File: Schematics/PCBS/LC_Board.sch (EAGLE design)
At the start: 7 parts, among them IC1 STP16C596M

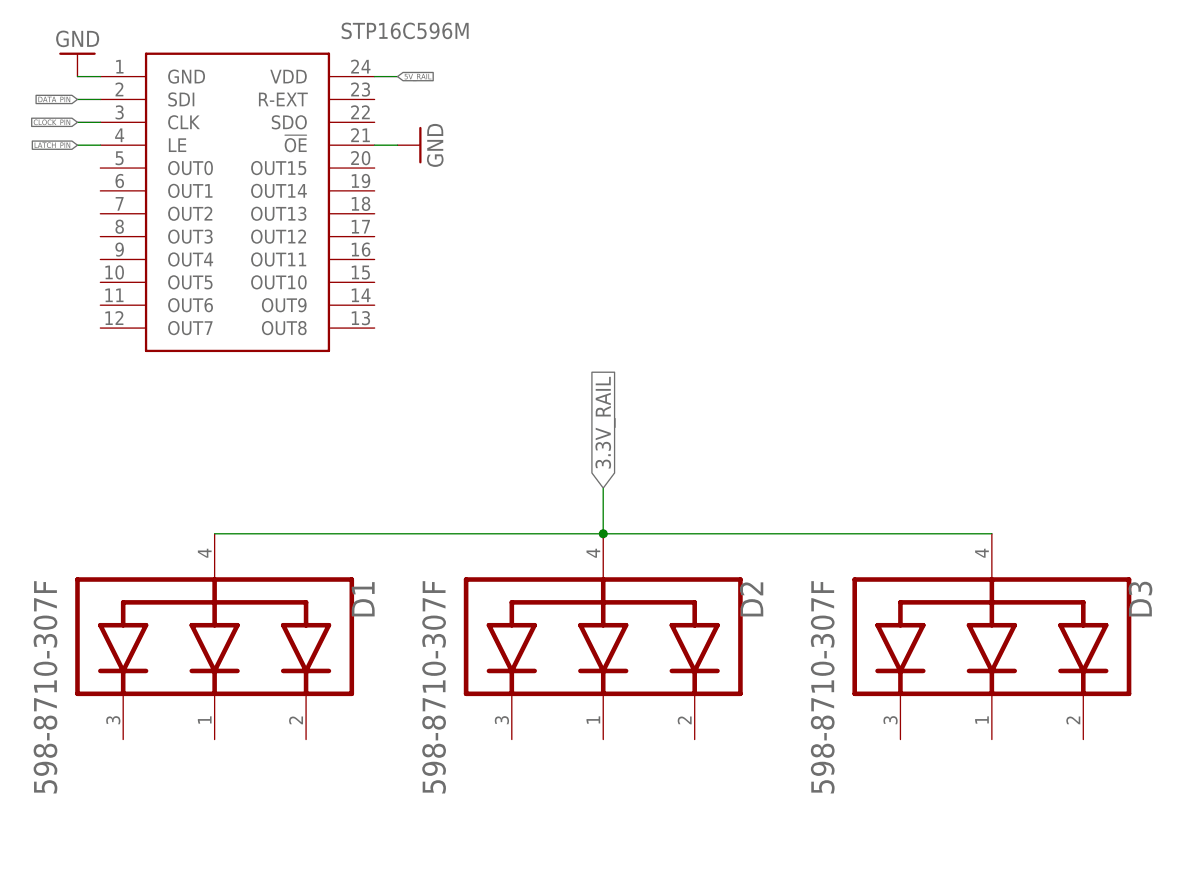
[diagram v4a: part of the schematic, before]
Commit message: connected LED & IO to Shift register
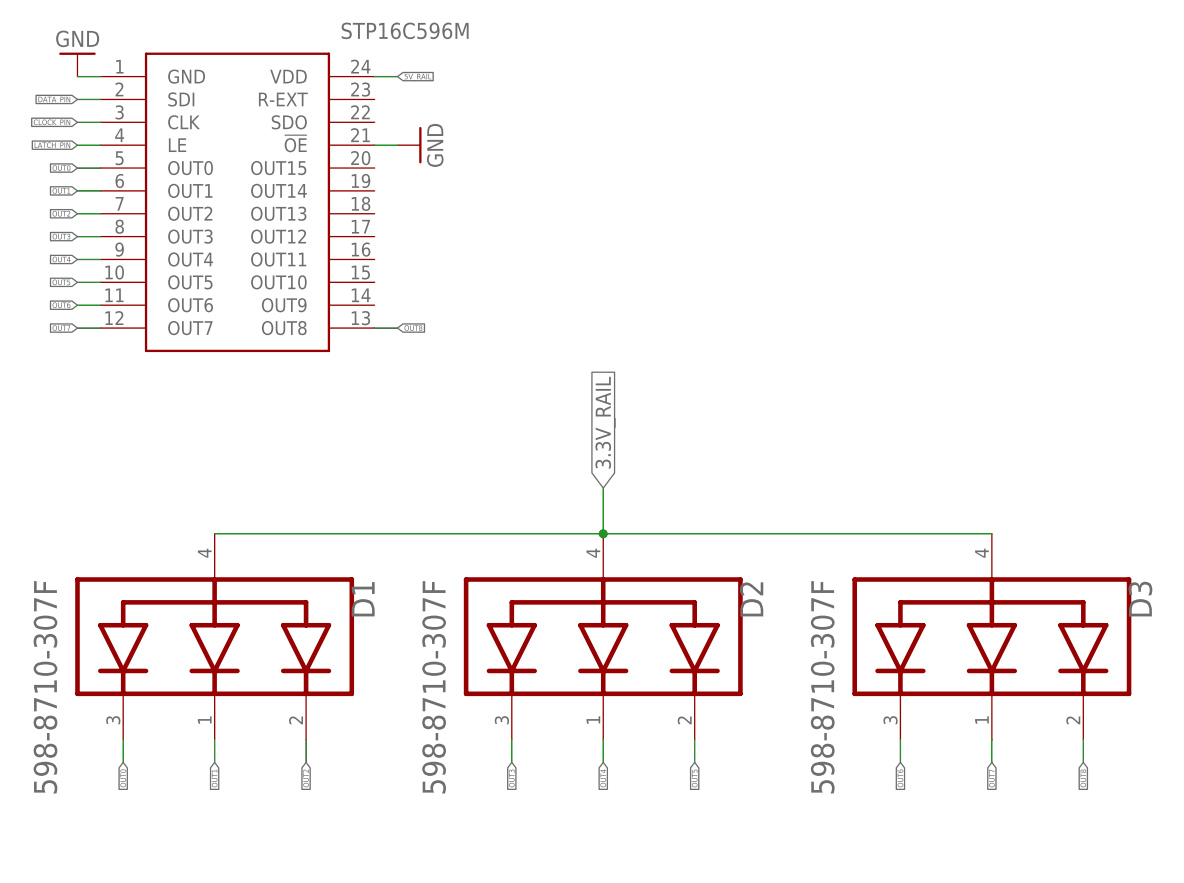
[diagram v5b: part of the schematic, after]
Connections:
- new net OUT0: D1.BLUE_CATHODE, IC1.OUT0
- new net OUT1: D1.GREEN_CATHODE, IC1.OUT1
- new net OUT2: D1.RED_CATHODE, IC1.OUT2
- new net OUT3: D2.BLUE_CATHODE, IC1.OUT3
- new net OUT4: D2.GREEN_CATHODE, IC1.OUT4
- new net OUT5: D2.RED_CATHODE, IC1.OUT5
- new net OUT6: D3.BLUE_CATHODE, IC1.OUT6
- new net OUT7: D3.GREEN_CATHODE, IC1.OUT7
- new net OUT8: D3.RED_CATHODE, IC1.OUT8
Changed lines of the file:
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@@
+</segment>
+</net>
+<net name="OUT0" class="0">
+<segment>
+<pinref part="IC1" gate="G$1" pin="OUT0"/>
+<wire x1="510.54" y1="0" x2="508" y2="0" width="0.1524" layer="91"/>
+<label x="508" y="0" size="0.6096" layer="95" rot="R180" xref="yes"/>
+</segment>
+<segment>
+<pinref part="D1" gate="G$0" pin="BLUE_CATHODE"/>
+<wire x1="513.08" y1="-63.5" x2="513.08" y2="-66.04" width="0.1524" layer="91"/>
+<label x="513.08" y="-66.04" size="0.6096" layer="95" rot="R270" xref="yes"/>
+</segment>
+</net>
+<net name="OUT1" class="0">
+<segment>
+<pinref part="IC1" gate="G$1" pin="OUT1"/>
+<wire x1="510.54" y1="-2.54" x2="508" y2="-2.54" width="0.1524" layer="91"/>
+<label x="508" y="-2.54" size="0.6096" layer="95" rot="R180" xref="yes"/>
+</segment>
+<segment>
+<pinref part="D1" gate="G$0" pin="GREEN_CATHODE"/>
+<wire x1="523.24" y1="-63.5" x2="523.24" y2="-66.04" width="0.1524" layer="91"/>
+<label x="523.24" y="-66.04" size="0.6096" layer="95" rot="R270" xref="yes"/>
+</segment>
+</net>
+<net name="OUT2" class="0">
+<segment>
+<pinref part="IC1" gate="G$1" pin="OUT2"/>
+<wire x1="510.54" y1="-5.08" x2="508" y2="-5.08" width="0.1524" layer="91"/>
+<label x="508" y="-5.08" size="0.6096" layer="95" rot="R180" xref="yes"/>
+</segment>
+<segment>
+<pinref part="D1" gate="G$0" pin="RED_CATHODE"/>
+<wire x1="533.4" y1="-63.5" x2="533.4" y2="-66.04" width="0.1524" layer="91"/>
+<label x="533.4" y="-66.04" size="0.6096" layer="95" rot="R270" xref="yes"/>
+</segment>
+</net>
+<net name="OUT3" class="0">
+<segment>
+<pinref part="IC1" gate="G$1" pin="OUT3"/>
+<wire x1="510.54" y1="-7.62" x2="508" y2="-7.62" width="0.1524" layer="91"/>
+<label x="508" y="-7.62" size="0.6096" layer="95" rot="R180" xref="yes"/>
+</segment>
+<segment>
+<pinref part="D2" gate="G$0" pin="BLUE_CATHODE"/>
+<wire x1="556.26" y1="-63.5" x2="556.26" y2="-66.04" width="0.1524" layer="91"/>
+<label x="556.26" y="-66.04" size="0.6096" layer="95" rot="R270" xref="yes"/>
+</segment>
+</net>
+<net name="OUT4" class="0">
+<segment>
+<pinref part="IC1" gate="G$1" pin="OUT4"/>
+<wire x1="510.54" y1="-10.16" x2="508" y2="-10.16" width="0.1524" layer="91"/>
+<label x="508" y="-10.16" size="0.6096" layer="95" rot="R180" xref="yes"/>
+</segment>
+<segment>
+<pinref part="D2" gate="G$0" pin="GREEN_CATHODE"/>
+<wire x1="566.42" y1="-63.5" x2="566.42" y2="-66.04" width="0.1524" layer="91"/>
+<label x="566.42" y="-66.04" size="0.6096" layer="95" rot="R270" xref="yes"/>
+</segment>
+</net>
+<net name="OUT5" class="0">
+<segment>
+<pinref part="D2" gate="G$0" pin="RED_CATHODE"/>
+<wire x1="576.58" y1="-63.5" x2="576.58" y2="-66.04" width="0.1524" layer="91"/>
+<label x="576.58" y="-66.04" size="0.6096" layer="95" rot="R270" xref="yes"/>
+</segment>
+<segment>
+<pinref part="IC1" gate="G$1" pin="OUT5"/>
+<wire x1="510.54" y1="-12.7" x2="508" y2="-12.7" width="0.1524" layer="91"/>
+<label x="508" y="-12.7" size="0.6096" layer="95" rot="R180" xref="yes"/>
+</segment>
+</net>
+<net name="OUT7" class="0">
+<segment>
+<pinref part="D3" gate="G$0" pin="GREEN_CATHODE"/>
+<wire x1="609.6" y1="-63.5" x2="609.6" y2="-66.04" width="0.1524" layer="91"/>
+<label x="609.6" y="-66.04" size="0.6096" layer="95" rot="R270" xref="yes"/>
+</segment>
+<segment>
+<pinref part="IC1" gate="G$1" pin="OUT7"/>
+<wire x1="510.54" y1="-17.78" x2="508" y2="-17.78" width="0.1524" layer="91"/>
+<label x="508" y="-17.78" size="0.6096" layer="95" rot="R180" xref="yes"/>
+</segment>
+</net>
+<net name="OUT8" class="0">
+<segment>
+<pinref part="D3" gate="G$0" pin="RED_CATHODE"/>
+<wire x1="619.76" y1="-63.5" x2="619.76" y2="-66.04" width="0.1524" layer="91"/>
+<label x="619.76" y="-66.04" size="0.6096" layer="95" rot="R270" xref="yes"/>
+</segment>
+<segment>
+<pinref part="IC1" gate="G$1" pin="OUT8"/>
+<wire x1="541.02" y1="-17.78" x2="543.56" y2="-17.78" width="0.1524" layer="91"/>
+<label x="543.56" y="-17.78" size="0.6096" layer="95" xref="yes"/>
+</segment>
+</net>
+<net name="OUT6" class="0">
+<segment>
+<pinref part="D3" gate="G$0" pin="BLUE_CATHODE"/>
+<wire x1="599.44" y1="-63.5" x2="599.44" y2="-66.04" width="0.1524" layer="91"/>
+<label x="599.44" y="-66.04" size="0.6096" layer="95" rot="R270" xref="yes"/>
+</segment>
+<segment>
+<pinref part="IC1" gate="G$1" pin="OUT6"/>
+<wire x1="510.54" y1="-15.24" x2="508" y2="-15.24" width="0.1524" layer="91"/>
+<label x="508" y="-15.24" size="0.6096" layer="95" rot="R180" xref="yes"/>
 </segment>
 </net>
